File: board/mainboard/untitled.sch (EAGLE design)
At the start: 1 part

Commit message: add brd
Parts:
- added RASPI: (no value), con-lstb:MA20-2
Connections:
- new net CAM_RX: RASPI.10, U$1.TX8/35
- new net CAM_TX: RASPI.8, U$1.RX8/34
- net +5V: now also RASPI.2, RASPI.4
- net GND: now also RASPI.6
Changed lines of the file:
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@@
 <setting verticaltext="up"/>
 </settings>
-<grid distance="0.1" unitdist="inch" unit="inch" style="lines" multiple="1" display="no" altdistance="0.01" altunitdist="inch" altunit="inch"/>
+<grid distance="0.1" unitdist="inch" unit="inch" style="lines" multiple="1" display="no" altdistance="0.05" altunitdist="inch" altunit="inch"/>
 <layers>
 <layer number="1" name="Top" color="4" fill="1" visible="no" active="no"/>
+<layer number="2" name="Route2" color="1" fill="3" visible="no" active="no"/>
+<layer number="3" name="Route3" color="4" fill="3" visible="no" active="no"/>
+<layer number="4" name="Route4" color="1" fill="4" visible="no" active="no"/>
+<layer number="5" name="Route5" color="4" fill="4" visible="no" active="no"/>
+<layer number="6" name="Route6" color="1" fill="8" visible="no" active="no"/>
+<layer number="7" name="Route7" color="4" fill="8" visible="no" active="no"/>
+<layer number="8" name="Route8" color="1" fill="2" visible="no" active="no"/>
+<layer number="9" name="Route9" color="4" fill="2" visible="no" active="no"/>
+<layer number="10" name="Route10" color="1" fill="7" visible="no" active="no"/>
+<layer number="11" name="Route11" color="4" fill="7" visible="no" active="no"/>
+<layer number="12" name="Route12" color="1" fill="5" visible="no" active="no"/>
+<layer number="13" name="Route13" color="4" fill="5" visible="no" active="no"/>
+<layer number="14" name="Route14" color="1" fill="6" visible="no" active="no"/>
+<layer number="15" name="Route15" color="4" fill="6" visible="no" active="no"/>
 <layer number="16" name="Bottom" color="1" fill="1" visible="no" active="no"/>
 <layer number="17" name="Pads" color="2" fill="1" visible="no" active="no"/>
@@
 <part name="P+1" library="supply1" library_urn="urn:adsk.eagle:library:371" deviceset="+5V" device=""/>
 <part name="GND1" library="supply1" library_urn="urn:adsk.eagle:library:371" deviceset="GND" device=""/>
+<part name="RASPI" library="con-lstb" library_urn="urn:adsk.eagle:library:162" deviceset="MA20-2" device="" package3d_urn="urn:adsk.eagle:package:8338/1"/>
+<part name="GND2" library="supply1" library_urn="urn:adsk.eagle:library:371" deviceset="GND" device=""/>
+<part name="P+2" library="supply1" library_urn="urn:adsk.eagle:library:371" deviceset="+5V" device=""/>
 </parts>
 <sheets>
@@
 </plain>
 <instances>
-<instance part="U$1" gate="G$1" x="38.1" y="64.77" smashed="yes"/>
-<instance part="P+1" gate="1" x="63.5" y="90.17" smashed="yes">
-<attribute name="VALUE" x="60.96" y="85.09" size="1.778" layer="96" rot="R90"/>
-</instance>
-<instance part="GND1" gate="1" x="76.2" y="72.39" smashed="yes">
-<attribute name="VALUE" x="73.66" y="69.85" size="1.778" layer="96"/>
+<instance part="U$1" gate="G$1" x="38.1" y="66.04" smashed="yes"/>
+<instance part="P+1" gate="1" x="63.5" y="91.44" smashed="yes">
+<attribute name="VALUE" x="60.96" y="86.36" size="1.778" layer="96" rot="R90"/>
+</instance>
+<instance part="GND1" gate="1" x="76.2" y="73.66" smashed="yes">
+<attribute name="VALUE" x="73.66" y="71.12" size="1.778" layer="96"/>
+</instance>
+<instance part="RASPI" gate="G$1" x="-38.1" y="73.66" smashed="yes" rot="R180">
+<attribute name="VALUE" x="-34.29" y="104.14" size="1.778" layer="96" rot="R180"/>
+<attribute name="NAME" x="-34.29" y="47.498" size="1.778" layer="95" rot="R180"/>
+</instance>
+<instance part="GND2" gate="1" x="0" y="86.36" smashed="yes">
+<attribute name="VALUE" x="-2.54" y="83.82" size="1.778" layer="96"/>
+</instance>
+<instance part="P+2" gate="1" x="-27.94" y="104.14" smashed="yes">
+<attribute name="VALUE" x="-30.48" y="99.06" size="1.778" layer="96" rot="R90"/>
 </instance>
 </instances>
@@
 <segment>
 <pinref part="U$1" gate="G$1" pin="GND"/>
-<wire x1="58.42" y1="77.47" x2="76.2" y2="77.47" width="0.1524" layer="91"/>
-<wire x1="76.2" y1="77.47" x2="76.2" y2="74.93" width="0.1524" layer="91"/>
+<wire x1="58.42" y1="78.74" x2="76.2" y2="78.74" width="0.1524" layer="91"/>
+<wire x1="76.2" y1="78.74" x2="76.2" y2="76.2" width="0.1524" layer="91"/>
 <pinref part="GND1" gate="1" pin="GND"/>
 </segment>
+<segment>
+<pinref part="GND2" gate="1" pin="GND"/>
+<pinref part="RASPI" gate="G$1" pin="6"/>
+<wire x1="0" y1="88.9" x2="0" y2="93.98" width="0.1524" layer="91"/>
+<wire x1="0" y1="93.98" x2="-30.48" y2="93.98" width="0.1524" layer="91"/>
+</segment>
 </net>
 <net name="+5V" class="0">
 <segment>
 <pinref part="U$1" gate="G$1" pin="VIN"/>
-<wire x1="58.42" y1="80.01" x2="63.5" y2="80.01" width="0.1524" layer="91"/>
-<wire x1="63.5" y1="80.01" x2="63.5" y2="87.63" width="0.1524" layer="91"/>
+<wire x1="58.42" y1="81.28" x2="63.5" y2="81.28" width="0.1524" layer="91"/>
+<wire x1="63.5" y1="81.28" x2="63.5" y2="88.9" width="0.1524" layer="91"/>
 <pinref part="P+1" gate="1" pin="+5V"/>
+</segment>
+<segment>
+<pinref part="RASPI" gate="G$1" pin="4"/>
+<wire x1="-30.48" y1="96.52" x2="-27.94" y2="96.52" width="0.1524" layer="91"/>
+<pinref part="P+2" gate="1" pin="+5V"/>
+<pinref part="RASPI" gate="G$1" pin="2"/>
+<wire x1="-27.94" y1="96.52" x2="-27.94" y2="99.06" width="0.1524" layer="91"/>
+<wire x1="-30.48" y1="99.06" x2="-27.94" y2="99.06" width="0.1524" layer="91"/>
+<wire x1="-27.94" y1="101.6" x2="-27.94" y2="99.06" width="0.1524" layer="91"/>
+</segment>
+</net>
+<net name="CAM_TX" class="0">
+<segment>
+<pinref part="RASPI" gate="G$1" pin="8"/>
+<wire x1="-30.48" y1="91.44" x2="-27.94" y2="91.44" width="0.1524" layer="91"/>
+<label x="-27.94" y="91.44" size="1.778" layer="95" xref="yes"/>
+</segment>
+<segment>
+<label x="68.58" y="25.4" size="1.778" layer="95" xref="yes"/>
+<wire x1="58.5724" y1="25.4" x2="63.5" y2="25.4" width="0.1524" layer="91"/>
+<pinref part="U$1" gate="G$1" pin="RX8/34"/>
+<wire x1="63.5" y1="25.4" x2="68.58" y2="25.4" width="0.1524" layer="91"/>
+<wire x1="58.5724" y1="25.4" x2="58.42" y2="25.4" width="0.1524" layer="91"/>
+</segment>
+</net>
+<net name="CAM_RX" class="0">
+<segment>
+<pinref part="RASPI" gate="G$1" pin="10"/>
+<wire x1="-30.48" y1="88.9" x2="-15.24" y2="88.9" width="0.1524" layer="91"/>
+<label x="-15.24" y="88.9" size="1.778" layer="95" xref="yes"/>
+</segment>
+<segment>
+<label x="81.28" y="27.94" size="1.778" layer="95" xref="yes"/>
+<wire x1="58.5724" y1="27.94" x2="60.96" y2="27.94" width="0.1524" layer="91"/>
+<pinref part="U$1" gate="G$1" pin="TX8/35"/>
+<wire x1="60.96" y1="27.94" x2="81.28" y2="27.94" width="0.1524" layer="91"/>
+<wire x1="58.42" y1="27.94" x2="58.5724" y2="27.94" width="0.1524" layer="91"/>
+</segment>
+</net>
+<net name="N$1" class="0">
+<segment>
+<wire x1="58.5724" y1="68.58" x2="60.8076" y2="68.58" width="0.1524" layer="91"/>
+</segment>
+</net>
+<net name="N$2" class="0">
+<segment>
+<wire x1="58.5724" y1="66.04" x2="60.8076" y2="66.04" width="0.1524" layer="91"/>
 </segment>
 </net>
@@
 will not be understood (or retained) with this version.
 </note>
+<note version="8.3" severity="warning">
+Since Version 8.3, EAGLE supports the association of 3D packages
+with devices in libraries, schematics, and board files. Those 3D
+packages will not be understood (or retained) with this version.
+</note>
 </compatibility>

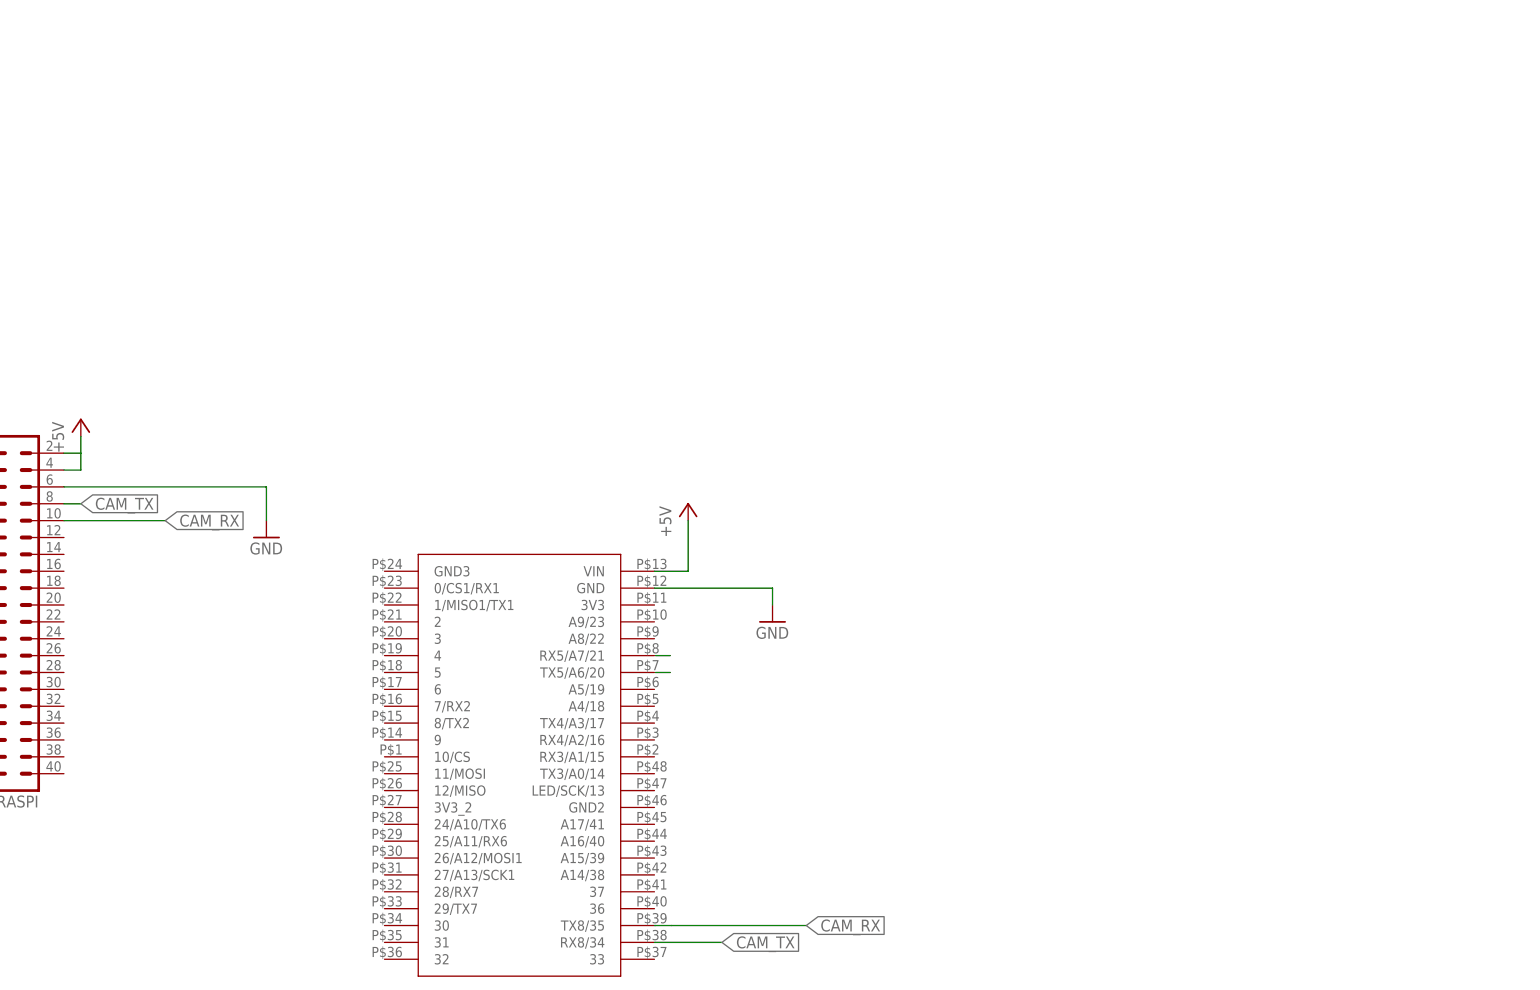
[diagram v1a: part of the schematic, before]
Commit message: add linesensor part
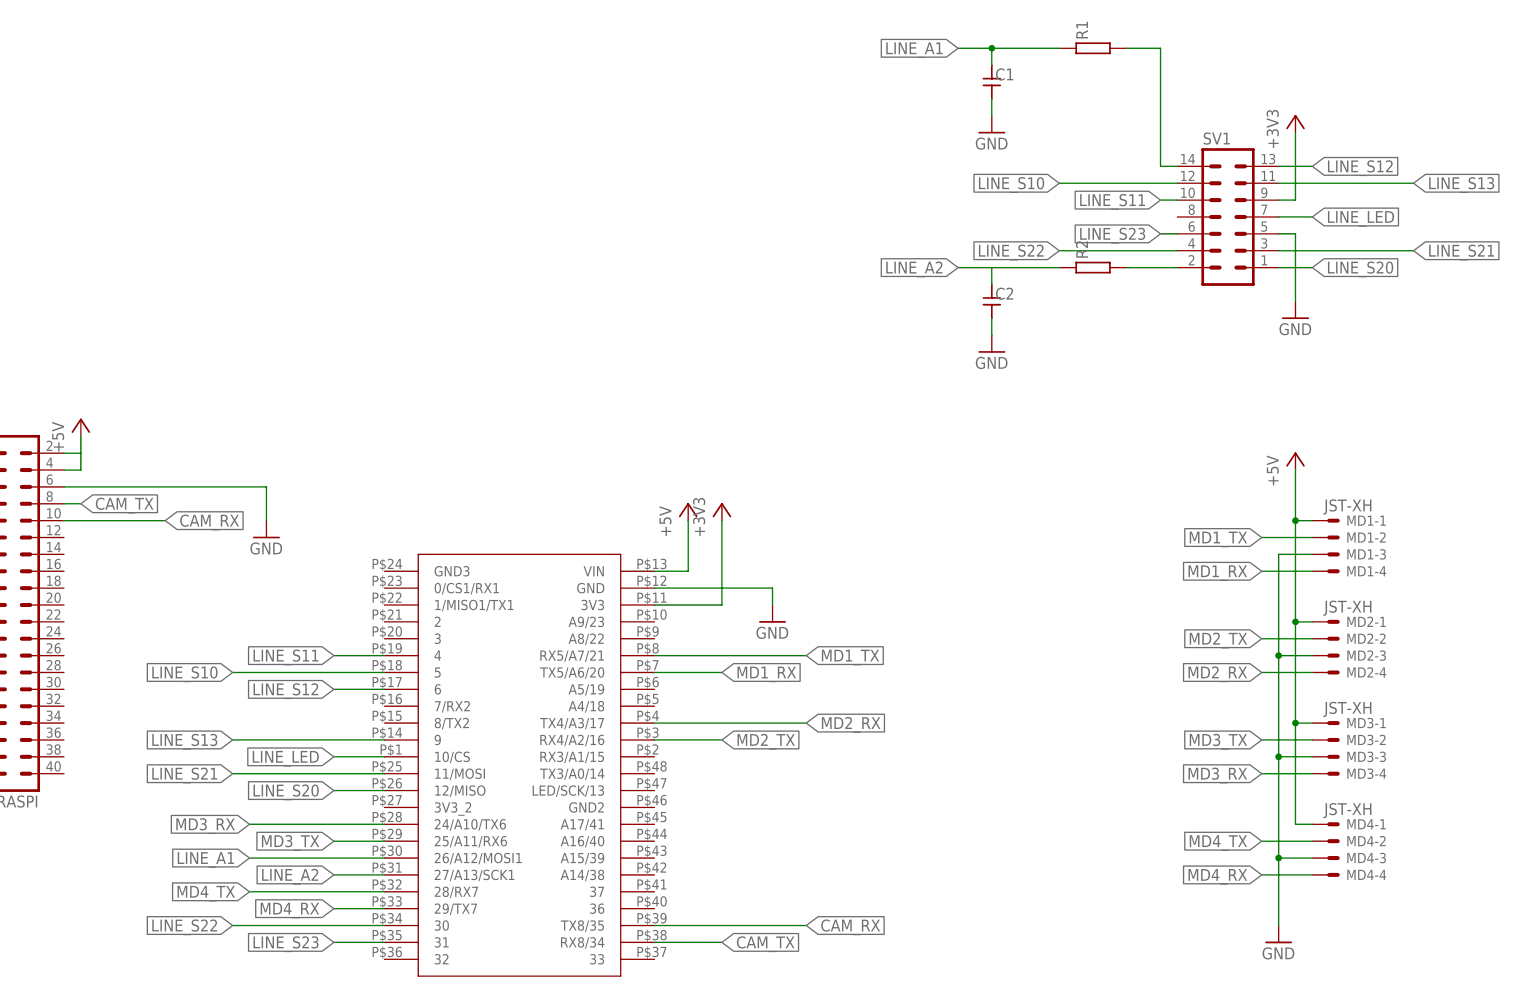
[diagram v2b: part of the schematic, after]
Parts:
- added C1, C2: (no value), generic:CAPACITOR1608
- added MD1, MD2, MD3, MD4: JST-XH, Rembrandt Electronics - JST XH Connectors v1-0:JST-XH-04-PIN-ROUND-PAD
- added R1, R2: (no value), generic:RESISTOR1608
- added SV1: (no value), con-lstb:MA07-2
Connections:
- new net +3V3: SV1.9, U$1.3V3
- new net LINE_A1: C1.1, R1.1, U$1.26/A12/MOSI1
- new net LINE_A2: C2.1, R2.1, U$1.27/A13/SCK1
- new net LINE_LED: SV1.7, U$1.10/CS
- new net LINE_S10: SV1.12, U$1.5
- new net LINE_S11: SV1.10, U$1.4
- new net LINE_S12: SV1.13, U$1.6
- new net LINE_S13: SV1.11, U$1.9
- new net LINE_S20: SV1.1, U$1.12/MISO
- new net LINE_S21: SV1.3, U$1.11/MOSI
- new net LINE_S22: SV1.4, U$1.30
- new net LINE_S23: SV1.6, U$1.31
- new net MD1_RX: MD1-4.S, U$1.TX5/A6/20
- new net MD1_TX: MD1-2.S, U$1.RX5/A7/21
- new net MD2_RX: MD2-4.S, U$1.TX4/A3/17
- new net MD2_TX: MD2-2.S, U$1.RX4/A2/16
- new net MD3_RX: MD3-4.S, U$1.24/A10/TX6
- new net MD3_TX: MD3-2.S, U$1.25/A11/RX6
- new net MD4_RX: MD4-4.S, U$1.29/TX7
- new net MD4_TX: MD4-2.S, U$1.28/RX7
- new net N$2: R1.2, SV1.14
- new net N$3: R2.2, SV1.2
- net +5V: now also MD1-1.S, MD2-1.S, MD3-1.S, MD4-1.S
- net GND: now also C1.2, C2.2, MD1-3.S, MD2-3.S, MD3-3.S, MD4-3.S, SV1.5

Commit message: add IR connector
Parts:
- added IR, IR1: (no value), pinhead:PINHD-1X8
- added Q1, Q2, Q3, Q4: (no value), adafruit:MOSFET-NREFLOW
- added R10, R3, R4, R5, R6, R7, R8, R9: (no value), generic:RESISTOR1608
- renumbered SV1 to LINE
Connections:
- new net GYRO_D+: IR1.2
- new net GYRO_D-: IR1.1
- new net GYRO_RESET: IR1.5
- new net GYRO_RX: Q4.S, R10.2
- new net GYRO_TX: Q3.S, R8.2
- new net IR_D+: IR.2
- new net IR_D-: IR.1
- new net IR_RESET: IR.5
- new net IR_RX: Q2.S, R6.2, U$1.TX3/A0/14
- new net IR_TX: Q1.S, R4.2, U$1.RX3/A1/15
- new net N$1: IR1.3, Q3.D, R7.2
- new net N$4: IR.3, Q1.D, R3.2
- new net N$5: IR1.4, Q4.D, R9.2
- new net N$6: IR.4, Q2.D, R5.2
- new net UVCC: IR.6, IR1.6
- net +3V3: now also Q1.G, Q2.G, Q3.G, Q4.G, R10.1, R4.1, R6.1, R8.1
- net +5V: now also IR.8, IR1.8, R3.1, R5.1, R7.1, R9.1
- net GND: now also IR.7, IR1.7

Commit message: add catch sensor
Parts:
- added Q5: (no value), adafruit:MOSFET-NREFLOW
- added R11, R12: (no value), generic:RESISTOR1608
- added X1: JST-XH-03-PIN-ROUND-PAD, Rembrandt Electronics - JST XH Connectors v1-0:JST-XH-03-PIN-ROUND-PAD
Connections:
- new net CATCH_1: Q5.S, R12.2
- new net N$9: Q5.D, R11.2, X1-3.S
- net +3V3: now also Q5.G, R12.1
- net +5V: now also R11.1, X1-1.S
- net GND: now also X1-2.S
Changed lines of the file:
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@@
 <part name="P+9" library="supply1" library_urn="urn:adsk.eagle:library:371" deviceset="+5V" device=""/>
 <part name="+3V6" library="supply1" library_urn="urn:adsk.eagle:library:371" deviceset="+3V3" device=""/>
+<part name="X1" library="Rembrandt Electronics - JST XH Connectors v1-0" deviceset="JST-XH-03-PIN" device="-ROUND-PAD"/>
+<part name="GND9" library="supply1" library_urn="urn:adsk.eagle:library:371" deviceset="GND" device=""/>
+<part name="P+10" library="supply1" library_urn="urn:adsk.eagle:library:371" deviceset="+5V" device=""/>
+<part name="Q5" library="adafruit" deviceset="MOSFET-N" device="REFLOW"/>
+<part name="R11" library="generic" deviceset="RESISTOR" device="1608"/>
+<part name="R12" library="generic" deviceset="RESISTOR" device="1608"/>
+<part name="P+11" library="supply1" library_urn="urn:adsk.eagle:library:371" deviceset="+5V" device=""/>
+<part name="+3V7" library="supply1" library_urn="urn:adsk.eagle:library:371" deviceset="+3V3" device=""/>
 </parts>
 <sheets>
@@
 <instance part="+3V6" gate="G$1" x="-93.98" y="137.16" smashed="yes">
 <attribute name="VALUE" x="-96.52" y="132.08" size="1.778" layer="96" rot="R90"/>
+</instance>
+<instance part="X1" gate="-1" x="162.56" y="-5.08" smashed="yes">
+<attribute name="NAME" x="165.1" y="-5.842" size="1.524" layer="95"/>
+<attribute name="VALUE" x="161.798" y="-3.683" size="1.778" layer="96"/>
+</instance>
+<instance part="X1" gate="-2" x="162.56" y="-7.62" smashed="yes">
+<attribute name="NAME" x="165.1" y="-8.382" size="1.524" layer="95"/>
+</instance>
+<instance part="X1" gate="-3" x="162.56" y="-10.16" smashed="yes">
+<attribute name="NAME" x="165.1" y="-10.922" size="1.524" layer="95"/>
+</instance>
+<instance part="GND9" gate="1" x="157.48" y="-17.78" smashed="yes">
+<attribute name="VALUE" x="154.94" y="-20.32" size="1.778" layer="96"/>
+</instance>
+<instance part="P+10" gate="1" x="157.48" y="5.08" smashed="yes">
+<attribute name="VALUE" x="154.94" y="0" size="1.778" layer="96" rot="R90"/>
+</instance>
+<instance part="Q5" gate="G$1" x="134.62" y="-27.94" smashed="yes" rot="R270">
+<attribute name="NAME" x="135.255" y="-33.02" size="1.27" layer="95" rot="R270"/>
+<attribute name="VALUE" x="133.35" y="-33.02" size="1.27" layer="96" rot="R270"/>
+</instance>
+<instance part="R11" gate="G$1" x="144.78" y="-25.4" smashed="yes">
+<attribute name="NAME" x="146.05" y="-22.86" size="1.778" layer="95" font="vector" rot="MR180"/>
+<attribute name="VALUE" x="146.05" y="-27.94" size="1.778" layer="96" font="vector"/>
+</instance>
+<instance part="R12" gate="G$1" x="124.46" y="-25.4" smashed="yes">
+<attribute name="NAME" x="125.73" y="-22.86" size="1.778" layer="95" font="vector" rot="MR180"/>
+<attribute name="VALUE" x="125.73" y="-27.94" size="1.778" layer="96" font="vector"/>
+</instance>
+<instance part="P+11" gate="1" x="144.78" y="-12.7" smashed="yes">
+<attribute name="VALUE" x="142.24" y="-17.78" size="1.778" layer="96" rot="R90"/>
+</instance>
+<instance part="+3V7" gate="G$1" x="124.46" y="-12.7" smashed="yes">
+<attribute name="VALUE" x="121.92" y="-17.78" size="1.778" layer="96" rot="R90"/>
 </instance>
 </instances>
@@
 <pinref part="GND8" gate="1" pin="GND"/>
 </segment>
+<segment>
+<pinref part="X1" gate="-2" pin="S"/>
+<wire x1="160.02" y1="-7.62" x2="157.48" y2="-7.62" width="0.1524" layer="91"/>
+<wire x1="157.48" y1="-7.62" x2="157.48" y2="-15.24" width="0.1524" layer="91"/>
+<pinref part="GND9" gate="1" pin="GND"/>
+</segment>
 </net>
 <net name="+5V" class="0">
@@
 <pinref part="P+9" gate="1" pin="+5V"/>
 </segment>
+<segment>
+<pinref part="X1" gate="-1" pin="S"/>
+<wire x1="160.02" y1="-5.08" x2="157.48" y2="-5.08" width="0.1524" layer="91"/>
+<wire x1="157.48" y1="-5.08" x2="157.48" y2="2.54" width="0.1524" layer="91"/>
+<pinref part="P+10" gate="1" pin="+5V"/>
+</segment>
+<segment>
+<pinref part="R11" gate="G$1" pin="1"/>
+<wire x1="144.78" y1="-20.32" x2="144.78" y2="-15.24" width="0.1524" layer="91"/>
+<pinref part="P+11" gate="1" pin="+5V"/>
+</segment>
 </net>
 <net name="CAM_TX" class="0">
@@
 <pinref part="+3V6" gate="G$1" pin="+3V3"/>
 </segment>
+<segment>
+<pinref part="R12" gate="G$1" pin="1"/>
+<wire x1="124.46" y1="-20.32" x2="124.46" y2="-17.78" width="0.1524" layer="91"/>
+<pinref part="Q5" gate="G$1" pin="G"/>
+<wire x1="124.46" y1="-17.78" x2="132.08" y2="-17.78" width="0.1524" layer="91"/>
+<wire x1="132.08" y1="-17.78" x2="132.08" y2="-25.4" width="0.1524" layer="91"/>
+<wire x1="124.46" y1="-17.78" x2="124.46" y2="-15.24" width="0.1524" layer="91"/>
+<junction x="124.46" y="-17.78"/>
+<pinref part="+3V7" gate="G$1" pin="+3V3"/>
+</segment>
 </net>
 <net name="LINE_LED" class="0">
@@
 </segment>
 </net>
+<net name="N$9" class="0">
+<segment>
+<pinref part="X1" gate="-3" pin="S"/>
+<wire x1="160.02" y1="-10.16" x2="149.86" y2="-10.16" width="0.1524" layer="91"/>
+<pinref part="Q5" gate="G$1" pin="D"/>
+<pinref part="R11" gate="G$1" pin="2"/>
+<wire x1="139.7" y1="-30.48" x2="144.78" y2="-30.48" width="0.1524" layer="91"/>
+<wire x1="144.78" y1="-30.48" x2="149.86" y2="-30.48" width="0.1524" layer="91"/>
+<junction x="144.78" y="-30.48"/>
+<wire x1="149.86" y1="-10.16" x2="149.86" y2="-30.48" width="0.1524" layer="91"/>
+</segment>
+</net>
+<net name="CATCH_1" class="0">
+<segment>
+<pinref part="R12" gate="G$1" pin="2"/>
+<pinref part="Q5" gate="G$1" pin="S"/>
+<wire x1="124.46" y1="-30.48" x2="129.54" y2="-30.48" width="0.1524" layer="91"/>
+<wire x1="124.46" y1="-30.48" x2="121.92" y2="-30.48" width="0.1524" layer="91"/>
+<junction x="124.46" y="-30.48"/>
+<label x="121.92" y="-30.48" size="1.778" layer="95" rot="R180" xref="yes"/>
+</segment>
+</net>

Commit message: なんか
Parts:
- added JP1, JP2, JP3, JP4: (no value), pinhead:PINHD-1X4
- added Q6: (no value), adafruit:MOSFET-NREFLOW
- added R13, R14: (no value), generic:RESISTOR1608
- added X2: JST-XH-04-PIN-ROUND-PAD, Rembrandt Electronics - JST XH Connectors v1-0:JST-XH-04-PIN-ROUND-PAD
- added X3: JST-XH-02-PIN-ROUND-PAD, Rembrandt Electronics - JST XH Connectors v1-0:JST-XH-02-PIN-ROUND-PAD
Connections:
- new net CATCH_2: Q6.S, R14.2
- new net N$10: JP2.4, JP4.2
- new net N$11: JP2.3, JP4.3
- new net N$7: Q6.D, R13.2, X2-3.S
- new net N$8: X2-1.S, X3-2.S
- new net USB_D+: JP3.3
- new net USB_D-: JP3.4
- net +3V3: now also Q6.G, R14.1
- net +5V: now also R13.1, X2-4.S, X3-1.S
- net GND: now also JP3.1, JP4.4, X2-2.S
- net GYRO_D+: now also JP1.1
- net GYRO_D-: now also JP1.2
- net IR_D+: now also JP2.1
- net IR_D-: now also JP2.2
- net UVCC: now also JP3.2, JP4.1
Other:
- moved on the sheet: RASPI
